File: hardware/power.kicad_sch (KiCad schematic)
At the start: 79 parts, among them Q1 BSN20, Q2 AO3415A, U3 SY8088, U4 SY8088, U5 SY8088, U6 SY8089A, U7 SY8113, U8 SY8088

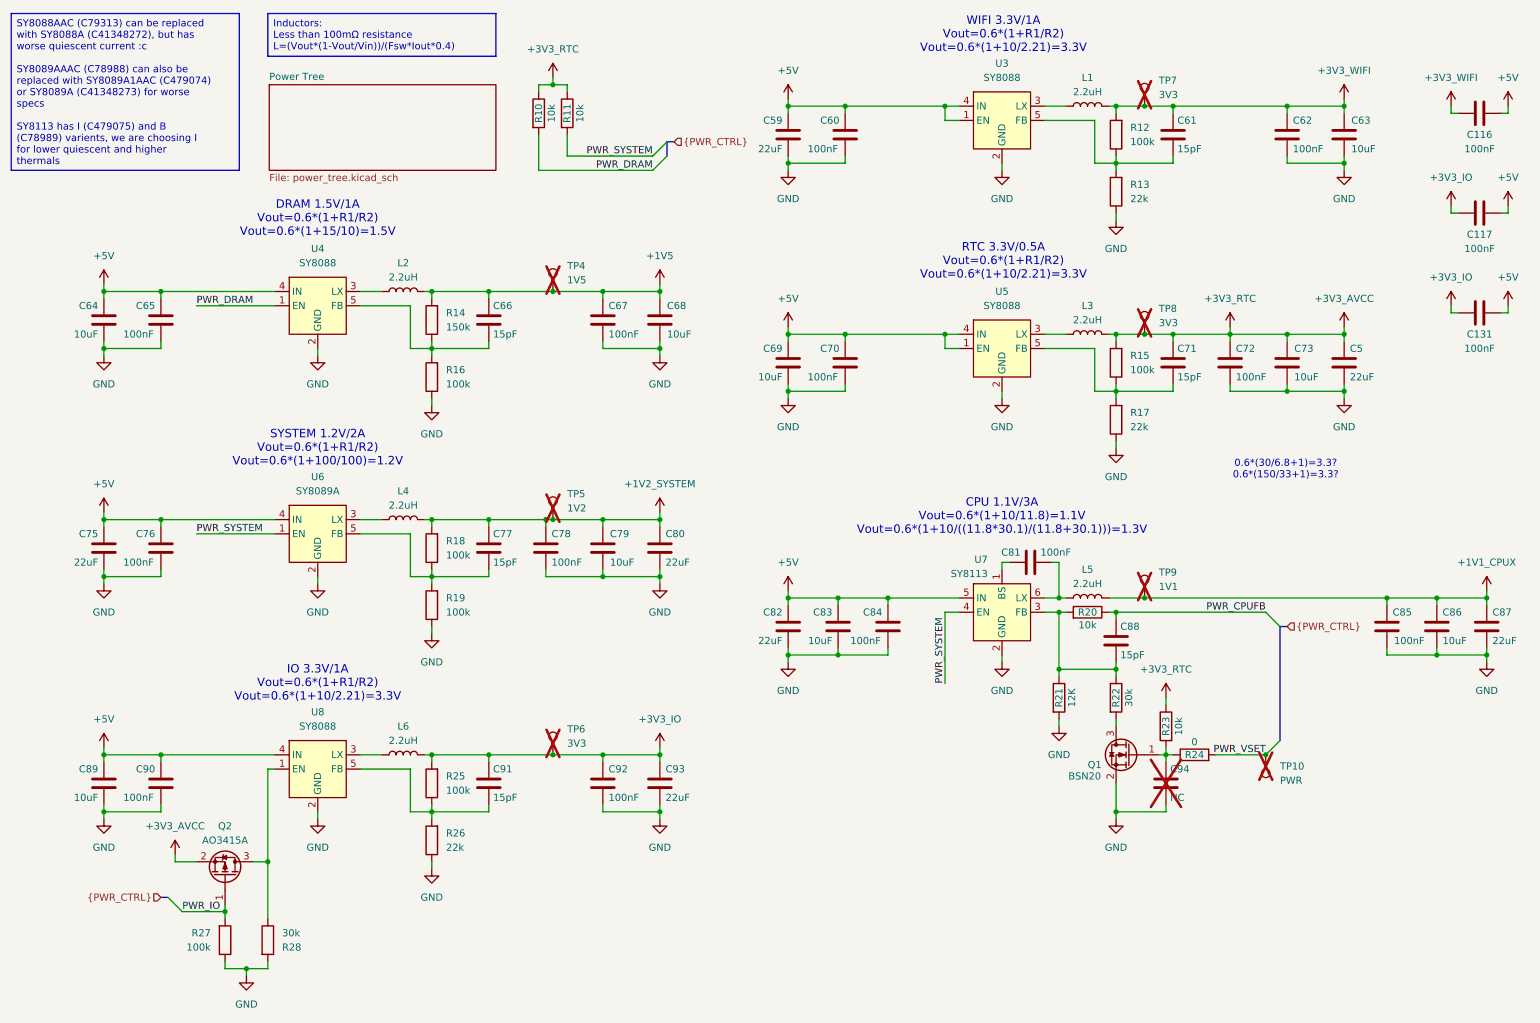
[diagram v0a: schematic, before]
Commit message: Improve heat dissipation and layout
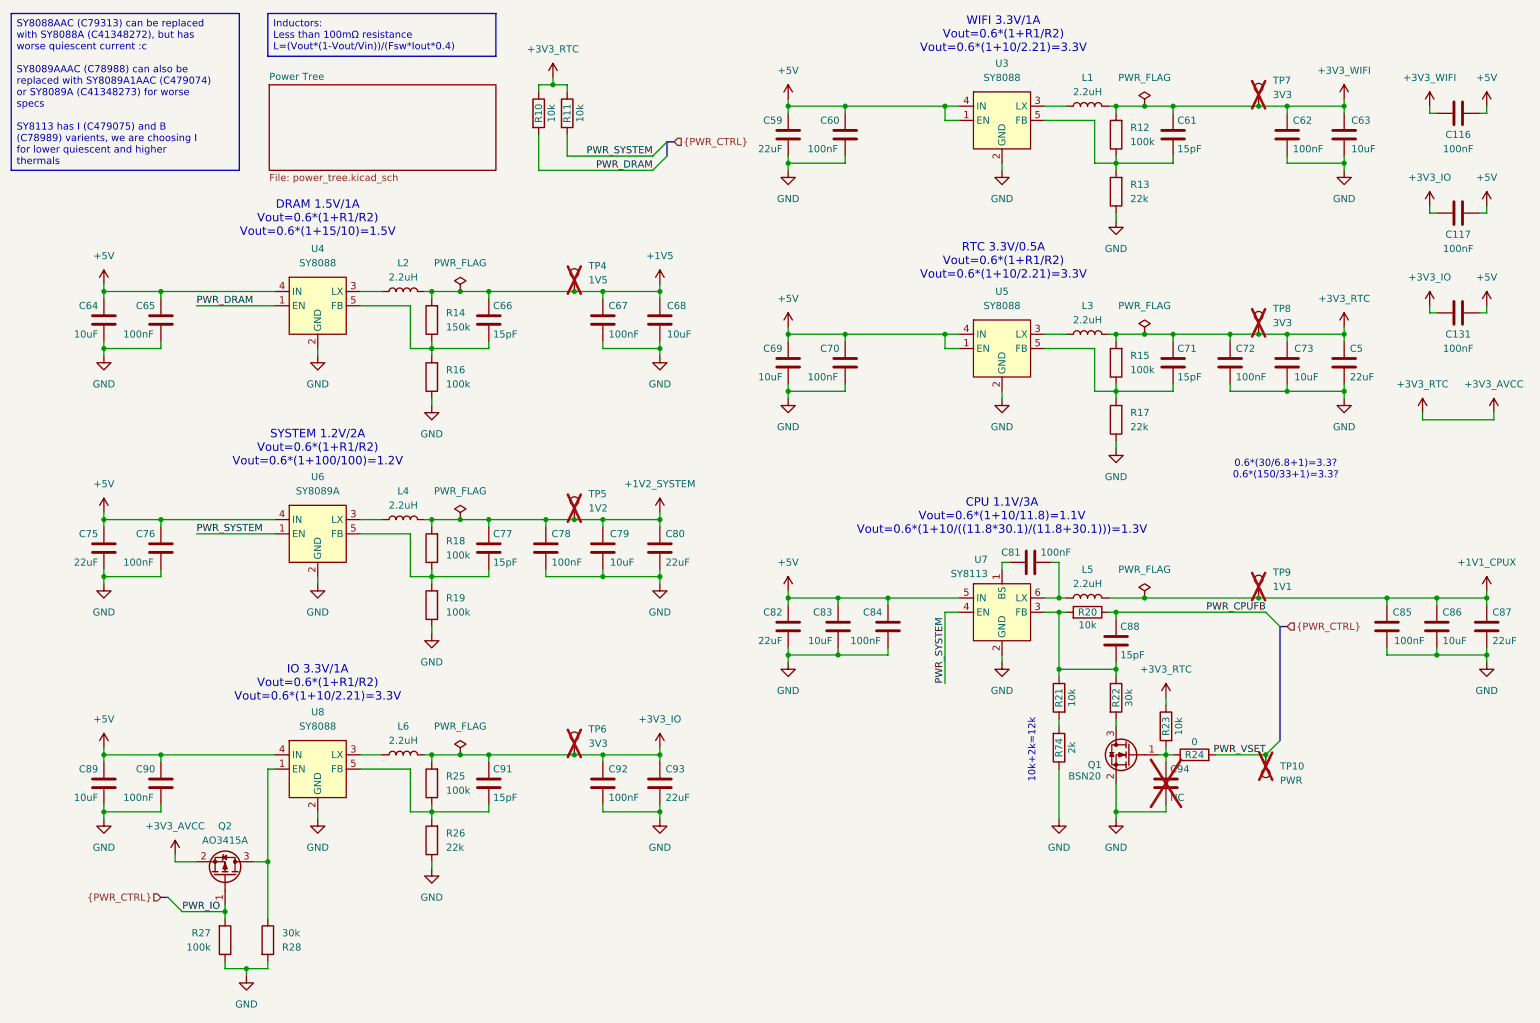
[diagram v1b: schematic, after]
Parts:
- added R74: 2k, Resistor_SMD:R_0402_1005Metric, symbol Device:R
- R21: value 12K -> 10k; LCSC Part # C25752 -> C25744
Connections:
- net GND: now also R74.1; no longer R21.2
- new net: R21.2, R74.2
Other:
- note added: "10k+2k=12k"
- moved on the sheet: C116, C117, C131, TP4, TP5, TP6, TP7, TP8, TP9
